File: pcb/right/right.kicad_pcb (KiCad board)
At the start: 2 copper layers, 163.5 x 132.8 mm, 66 parts

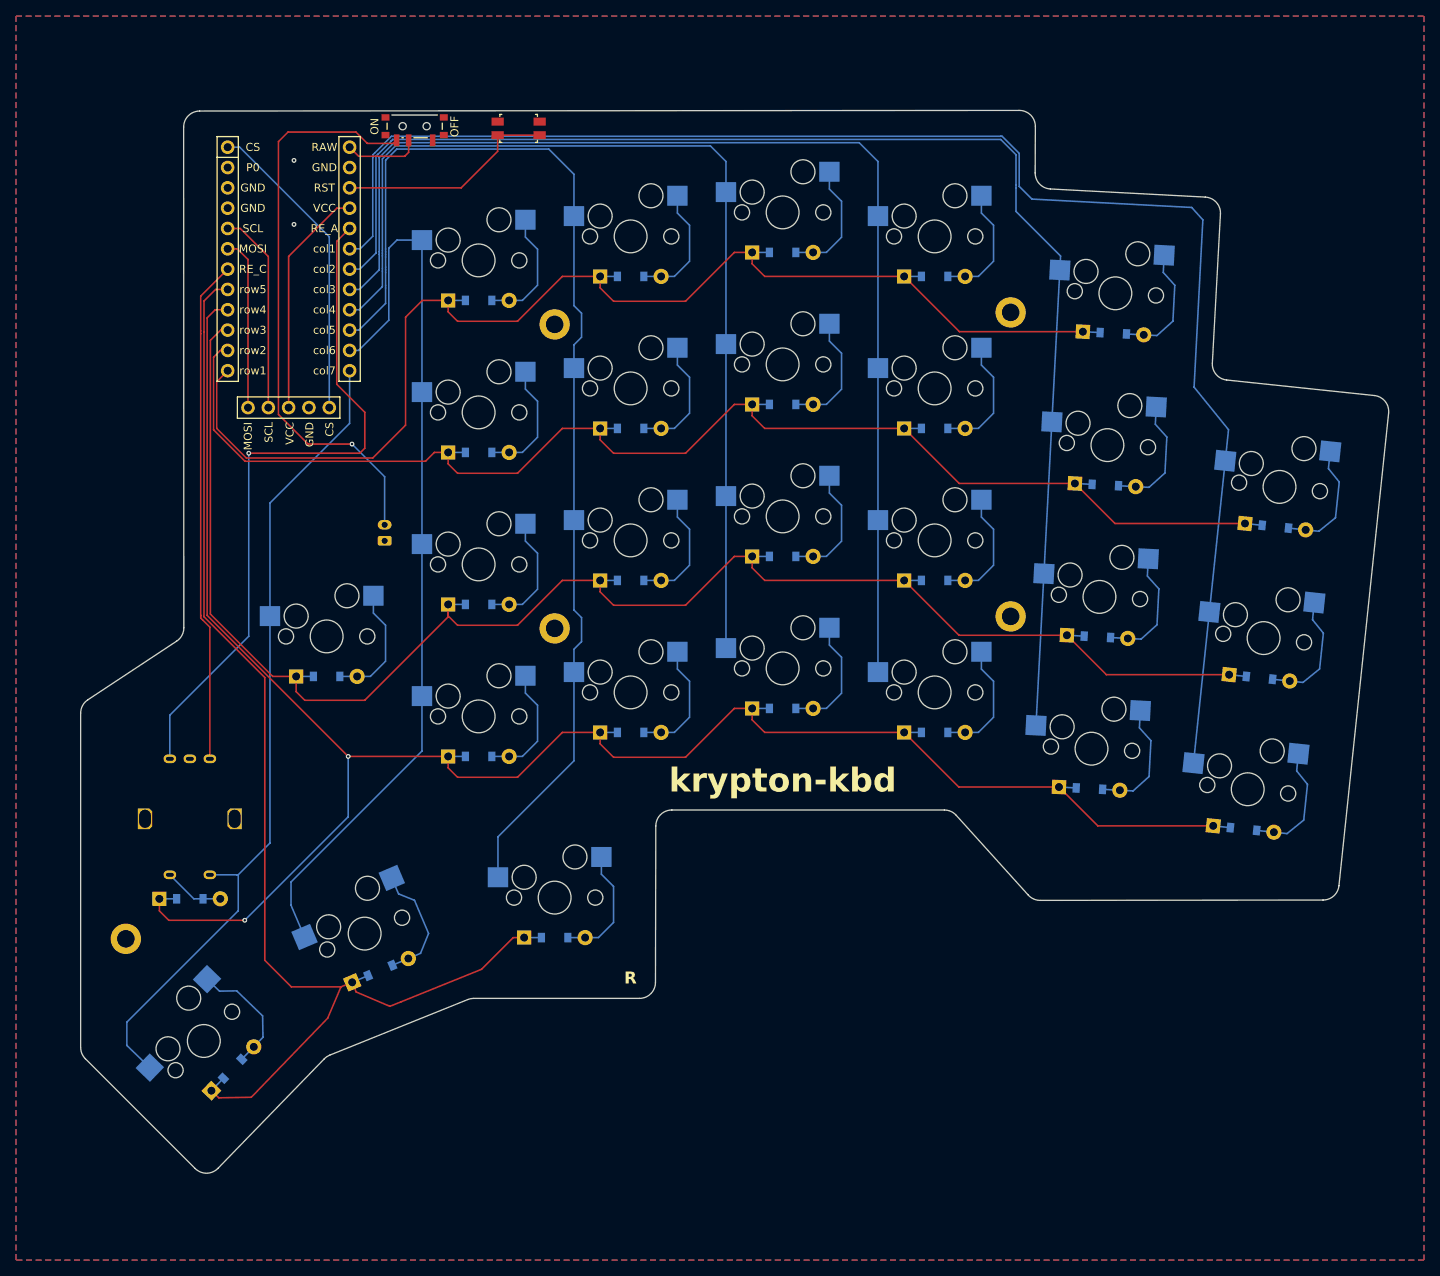
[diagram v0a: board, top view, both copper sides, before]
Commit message: Refined pcb routing, fixed hole issue on pcb
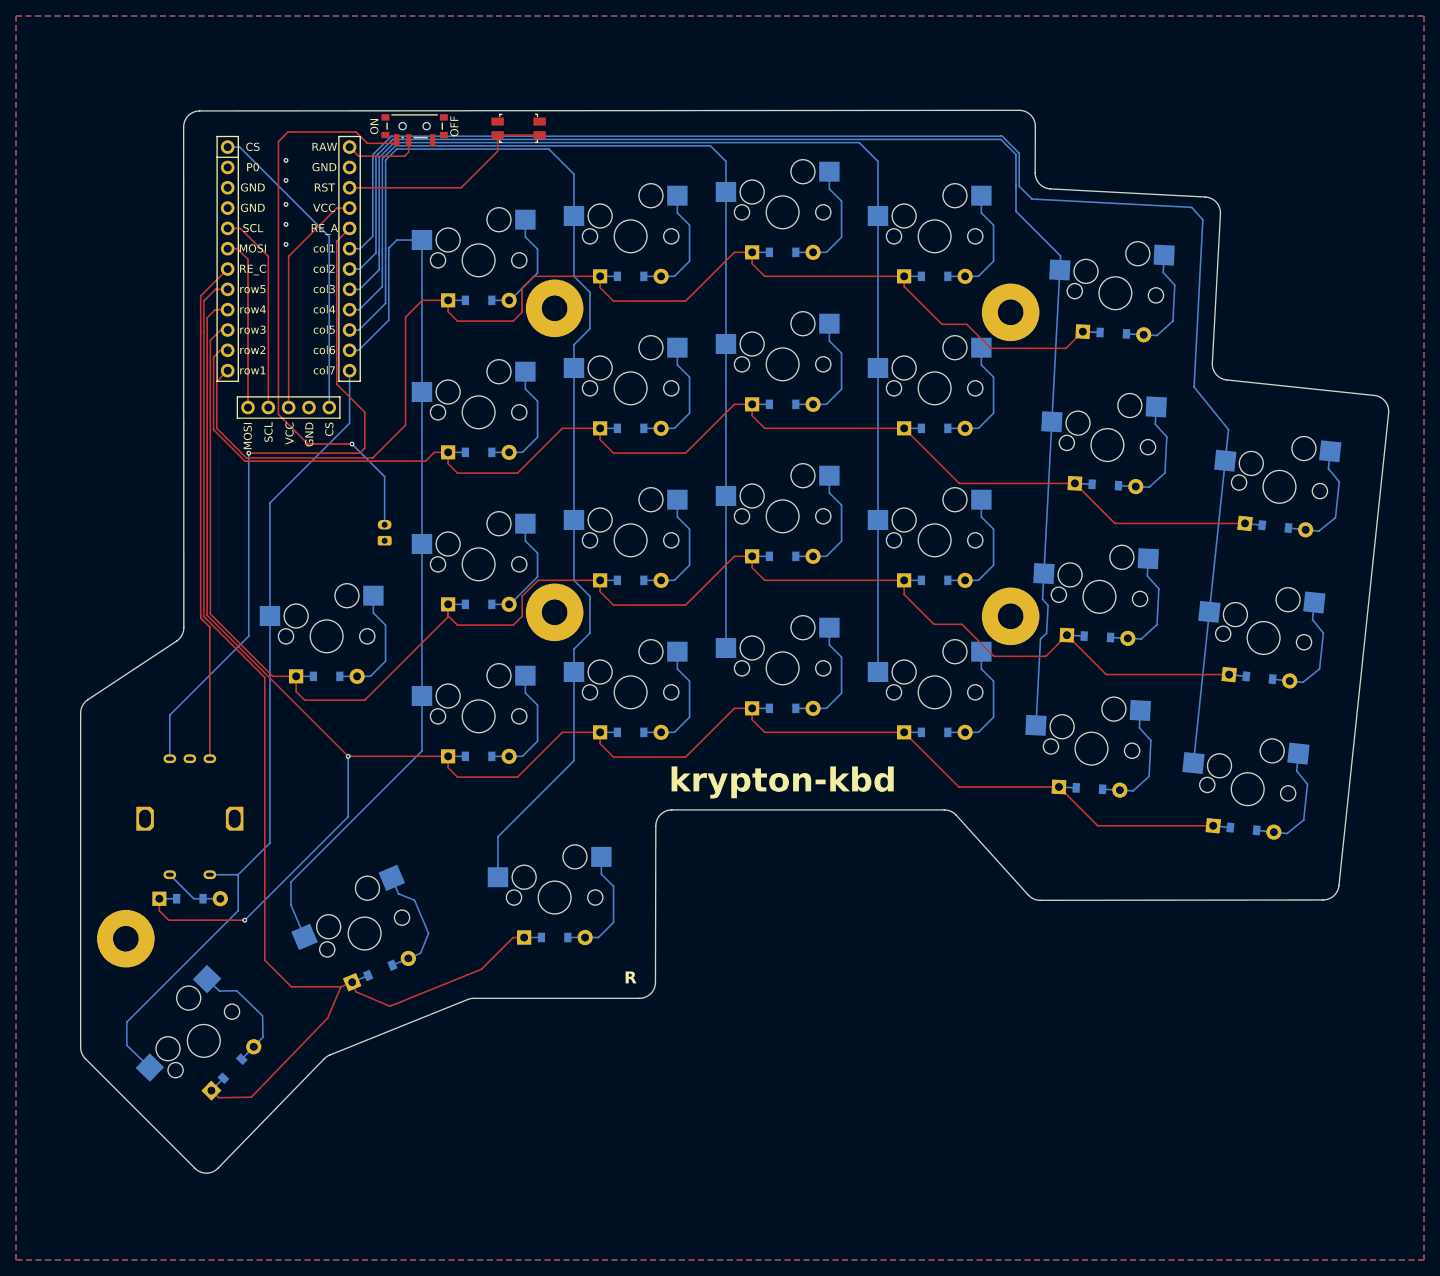
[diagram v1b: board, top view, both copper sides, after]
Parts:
- moved H3 2.01 mm to (190.6, 101.0)
- moved H4 2.01 mm to (190.6, 139.0)
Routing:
- net row3: track 206.7 -> 211.4 mm
- net row1: track 158.3 -> 162.5 mm
- net col5: track 142.6 -> 144.3 mm
- net mirror_inner_home: track 15.3 -> 14.4 mm
- net mirror_inner_num: track 15.3 -> 14.4 mm
- net col2: track 171.6 -> 172.2 mm
- net GND: vias 2 -> 5
